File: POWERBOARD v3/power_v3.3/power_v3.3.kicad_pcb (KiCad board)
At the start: 4 copper layers, 60 x 34.1 mm, 63 parts, among them IC1 MAX25301AATB_V+T, IC2 MCP6541T-I_OT, IC3 AP2281-1FMG-7, J1 43650-0300, J2 UJ20-C-H-G-SMT-1-P16-TR, J3 2053380002, U1 USBLC6-2, U2 BQ25886RGE, U3 TPS62160DSG

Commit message: Update PowerBoard
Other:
- board text added: "Power Board"

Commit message: Fixed D3 symbol
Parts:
- moved D3 0.43 mm to (163.6, 92.9)
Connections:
- D3 pad 2: GND -> unconnected-(D3-A2-Pad2)
- D3 pad 3: (no net) -> GND

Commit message: Fixed short on NTC-TS
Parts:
- D3: value SOD323 -> ESDS452DBZRQ1
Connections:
- R6 pad 1: NTC -> TS
- R7 pad 2: NTC -> TS
- S2 pad 5: NTC -> TS
- U2 pad 7: NTC -> TS
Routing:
- net NTC: track 47.3 -> 18.5 mm, vias 1 -> 0
- net TS: track 0.00 -> 28.3 mm, vias 0 -> 1
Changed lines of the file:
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@@
 		(capping no)
 		(filling no)
+		(zone_defaults)
 		(pcbplotparams
 			(layerselection 0x00000000_00000000_55555555_5755f5ff)
@@
 			(layers "*.Cu" "*.Mask")
 			(remove_unused_layers no)
-			(net "NTC")
+			(net "TS")
 			(pinfunction "COM_2_5")
 			(pintype "passive")
@@
 			(layers "F.Cu" "F.Mask" "F.Paste")
 			(roundrect_rratio 0.25)
-			(net "NTC")
+			(net "TS")
 			(pinfunction "TS_7")
 			(pintype "input")
@@
 			)
 		)
-		(property "Value" "SOD323"
+		(property "Value" "ESDS452DBZRQ1"
 			(at 0 -2.4 0)
 			(layer "B.Fab")
@@
 			(layers "B.Cu" "B.Mask" "B.Paste")
 			(roundrect_rratio 0.25)
-			(net "NTC")
+			(net "TS")
 			(pintype "passive")
 		)
@@
 			(layers "B.Cu" "B.Mask" "B.Paste")
 			(roundrect_rratio 0.25)
-			(net "NTC")
+			(net "TS")
 			(pintype "passive")
 		)
@@
 	)
 	(segment
-		(start 153.965 98.165)
-		(end 154.05 98.25)
-		(width 0.2)
-		(layer "F.Cu")
-		(net "NTC")
-	)
-	(segment
-		(start 152.015 95.015)
-		(end 153.1 96.1)
-		(width 0.2)
-		(layer "F.Cu")
-		(net "NTC")
-	)
-	(segment
-		(start 154.4 96.1)
-		(end 154.4 98.6)
-		(width 0.2)
-		(layer "F.Cu")
-		(net "NTC")
-	)
-	(segment
-		(start 178.1 95.315)
-		(end 178.575 94.84)
-		(width 0.2)
-		(layer "F.Cu")
-		(net "NTC")
-	)
-	(segment
-		(start 177.5 95.315)
-		(end 178.1 95.315)
+		(start 152 95.015)
+		(end 152 96.2)
 		(width 0.2)
 		(layer "F.Cu")
@@
 	)
 	(segment
-		(start 152 95.015)
-		(end 152.015 95.015)
+		(start 153.965 98.165)
+		(end 154.05 98.25)
 		(width 0.2)
 		(layer "F.Cu")
@@
 	)
 	(segment
-		(start 153.1 96.1)
-		(end 154.05 96.1)
+		(start 152 96.2)
+		(end 154.4 98.6)
 		(width 0.2)
 		(layer "F.Cu")
@@
 		(net "NTC")
 	)
-	(via
-		(at 177.5 95.315)
-		(size 0.6)
-		(drill 0.3)
-		(layers "F.Cu" "B.Cu")
-		(net "NTC")
-	)
-	(segment
-		(start 176.5 95.49)
-		(end 176.325 95.315)
-		(width 0.2)
-		(layer "B.Cu")
-		(net "NTC")
-	)
-	(segment
-		(start 155.75 94.75)
-		(end 163.986471 94.75)
-		(width 0.2)
-		(layer "B.Cu")
-		(net "NTC")
-	)
-	(segment
-		(start 176.5 97.315)
-		(end 176.5 97.777352)
-		(width 0.2)
-		(layer "B.Cu")
-		(net "NTC")
-	)
-	(segment
-		(start 176.325 95.315)
-		(end 177.5 95.315)
-		(width 0.2)
-		(layer "B.Cu")
-		(net "NTC")
-	)
-	(segment
-		(start 176.5 97.315)
-		(end 176.5 95.49)
-		(width 0.2)
-		(layer "B.Cu")
-		(net "NTC")
-	)
-	(segment
-		(start 165.326471 96.09)
-		(end 175.55 96.09)
-		(width 0.2)
-		(layer "B.Cu")
-		(net "NTC")
-	)
-	(segment
-		(start 163.986471 94.75)
-		(end 165.326471 96.09)
-		(width 0.2)
-		(layer "B.Cu")
-		(net "NTC")
-	)
-	(segment
-		(start 154.4 96.1)
-		(end 155.75 94.75)
-		(width 0.2)
-		(layer "B.Cu")
-		(net "NTC")
-	)
-	(segment
-		(start 175.55 96.09)
-		(end 176.325 95.315)
-		(width 0.2)
-		(layer "B.Cu")
-		(net "NTC")
-	)
 	(segment
 		(start 158.4 96.1)
@@
 		(net "Net-(U3-PG)")
 	)
+	(segment
+		(start 178.1 95.315)
+		(end 178.575 94.84)
+		(width 0.2)
+		(layer "F.Cu")
+		(net "TS")
+	)
+	(segment
+		(start 177.5 95.315)
+		(end 178.1 95.315)
+		(width 0.2)
+		(layer "F.Cu")
+		(net "TS")
+	)
+	(via
+		(at 177.5 95.315)
+		(size 0.6)
+		(drill 0.3)
+		(layers "F.Cu" "B.Cu")
+		(net "TS")
+	)
+	(segment
+		(start 155.75 94.75)
+		(end 170.739852 94.75)
+		(width 0.2)
+		(layer "B.Cu")
+		(net "TS")
+	)
+	(segment
+		(start 176.5 95.49)
+		(end 176.325 95.315)
+		(width 0.2)
+		(layer "B.Cu")
+		(net "TS")
+	)
+	(segment
+		(start 175.55 96.09)
+		(end 176.325 95.315)
+		(width 0.2)
+		(layer "B.Cu")
+		(net "TS")
+	)
+	(segment
+		(start 172.079852 96.09)
+		(end 175.55 96.09)
+		(width 0.2)
+		(layer "B.Cu")
+		(net "TS")
+	)
+	(segment
+		(start 154.4 96.1)
+		(end 155.75 94.75)
+		(width 0.2)
+		(layer "B.Cu")
+		(net "TS")
+	)
+	(segment
+		(start 176.5 97.315)
+		(end 176.5 97.777352)
+		(width 0.2)
+		(layer "B.Cu")
+		(net "TS")
+	)
+	(segment
+		(start 176.325 95.315)
+		(end 177.5 95.315)
+		(width 0.2)
+		(layer "B.Cu")
+		(net "TS")
+	)
+	(segment
+		(start 176.5 97.315)
+		(end 176.5 95.49)
+		(width 0.2)
+		(layer "B.Cu")
+		(net "TS")
+	)
+	(segment
+		(start 170.739852 94.75)
+		(end 172.079852 96.09)
+		(width 0.2)
+		(layer "B.Cu")
+		(net "TS")
+	)
 	(zone

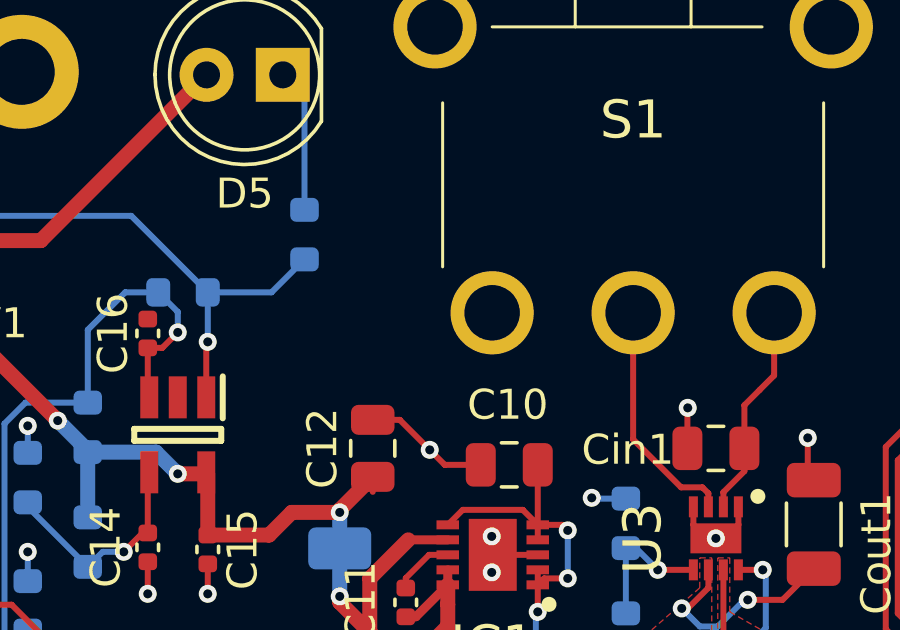
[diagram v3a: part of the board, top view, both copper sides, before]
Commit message: Changed S1 pin 1 from no connect to passive, connected to gnd on layout to follow schematic
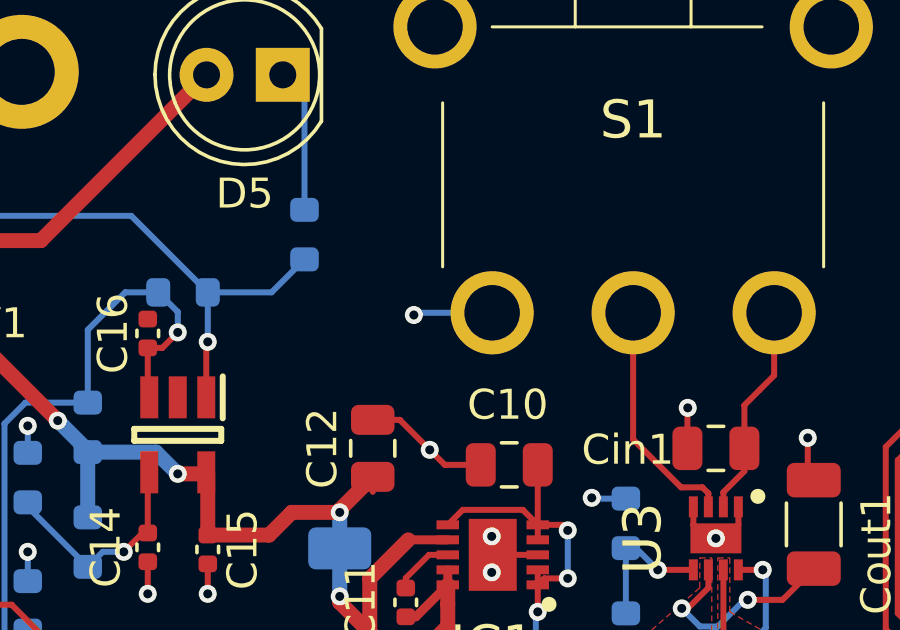
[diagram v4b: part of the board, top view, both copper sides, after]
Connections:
- S1 pad 1: unconnected-(S1-NC-Pad1) -> GND
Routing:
- net GND: track 65.0 -> 67.7 mm, vias 37 -> 38
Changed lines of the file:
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@@
 			(layers "*.Cu" "*.Mask")
 			(remove_unused_layers no)
-			(net "unconnected-(S1-NC-Pad1)")
+			(net "GND")
 			(pinfunction "NC_1")
-			(pintype "no_connect")
+			(pintype "passive")
 		)
 		(pad "2" thru_hole circle
@@
 	)
 	(via
+		(at 160.87 80.82)
+		(size 0.6)
+		(drill 0.3)
+		(layers "F.Cu" "B.Cu")
+		(free yes)
+		(net "GND")
+	)
+	(via
 		(at 156.2 93)
 		(size 0.6)
@@
 	)
 	(segment
+		(start 160.944 80.746)
+		(end 163.4795 80.746)
+		(width 0.2)
+		(layer "B.Cu")
+		(net "GND")
+	)
+	(segment
 		(start 161.36 92.93)
 		(end 162.5725 92.93)
@@
 		(width 0.2)
 		(layer "B.Cu")
+		(net "GND")
+	)
+	(segment
+		(start 160.87 80.82)
+		(end 160.944 80.746)
+		(width 0.2)
+		(layer "B.Cu")
